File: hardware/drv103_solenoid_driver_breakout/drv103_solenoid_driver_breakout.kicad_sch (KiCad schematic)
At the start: 26 parts, among them J1 DC IN, J2 CONTROL, J3 Solenoid, U1 DRV103U

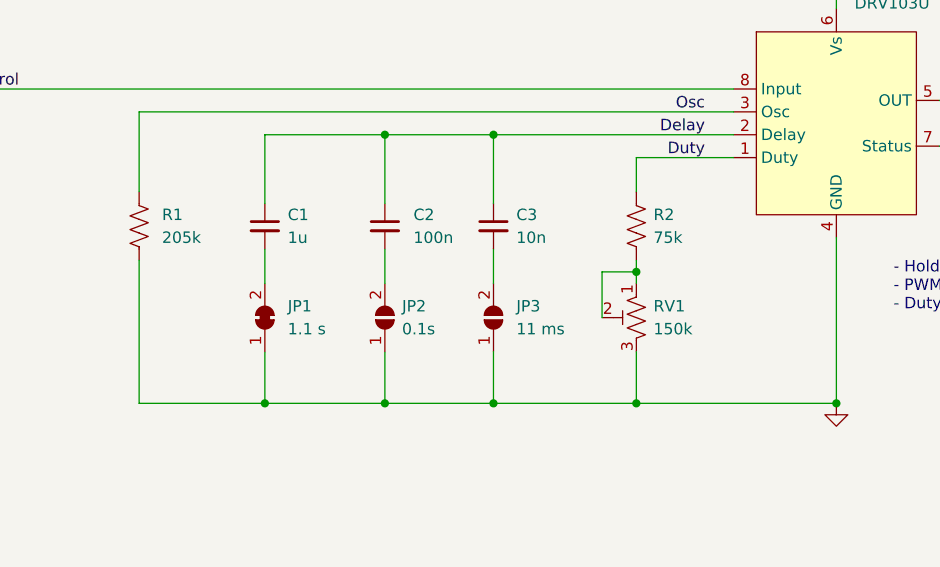
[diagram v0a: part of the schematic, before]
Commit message: Add actual component values
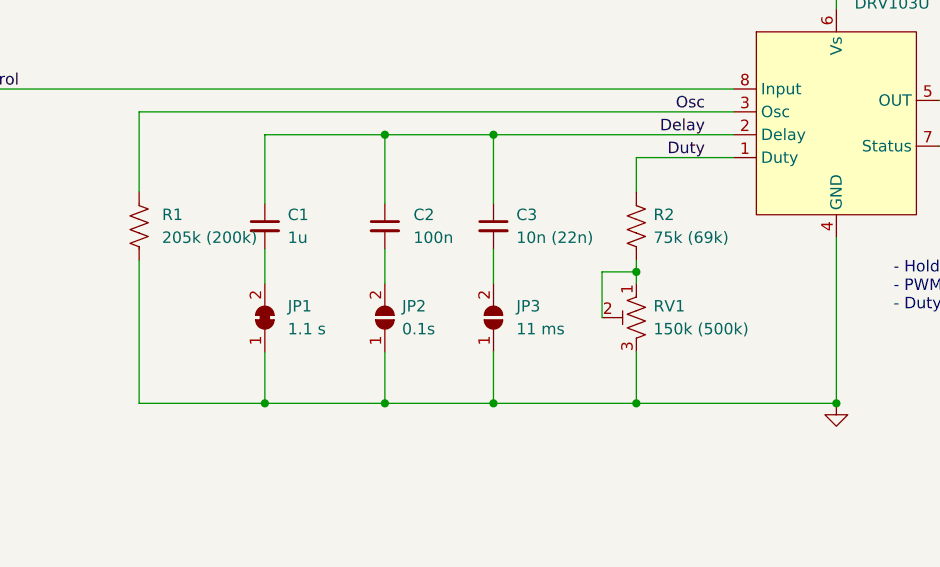
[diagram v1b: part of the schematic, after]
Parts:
- C3: value 10n -> 10n (22n)
- R1: value 205k -> 205k (200k)
- R2: value 75k -> 75k (69k)
- RV1: value 150k -> 150k (500k)
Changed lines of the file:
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@@
       (effects (font (size 1.27 1.27)) (justify right))
     )
-    (property "Value" "75k" (id 1) (at 130.81 106.0449 0)
+    (property "Value" "75k (69k)" (id 1) (at 130.81 106.0449 0)
       (effects (font (size 1.27 1.27)) (justify right))
     )
@@
       (effects (font (size 1.27 1.27)) (justify left))
     )
-    (property "Value" "10n" (id 1) (at 115.57 106.0512 0)
+    (property "Value" "10n (22n)" (id 1) (at 115.57 106.0512 0)
       (effects (font (size 1.27 1.27)) (justify left))
     )
@@
       (effects (font (size 1.27 1.27)) (justify right))
     )
-    (property "Value" "205k" (id 1) (at 76.2 106.0449 0)
+    (property "Value" "205k (200k)" (id 1) (at 76.2 106.0449 0)
       (effects (font (size 1.27 1.27)) (justify right))
     )
@@
       (effects (font (size 1.27 1.27)) (justify right))
     )
-    (property "Value" "150k" (id 1) (at 130.81 116.2049 0)
+    (property "Value" "150k (500k)" (id 1) (at 130.81 116.2049 0)
       (effects (font (size 1.27 1.27)) (justify right))
     )
@@
     )
     (path "/83963a71-109d-4df7-b582-2124aeaa82fb"
-      (reference "C3") (unit 1) (value "10n") (footprint "Capacitor_SMD:C_0603_1608Metric_Pad1.08x0.95mm_HandSolder")
+      (reference "C3") (unit 1) (value "10n (22n)") (footprint "Capacitor_SMD:C_0603_1608Metric_Pad1.08x0.95mm_HandSolder")
     )
     (path "/0f9a5fd2-781b-4164-bc3e-87cb4b11114a"
@@
     )
     (path "/cd5d6ec1-33a5-47ef-8204-cc6fc4d30391"
-      (reference "R1") (unit 1) (value "205k") (footprint "Resistor_SMD:R_0603_1608Metric_Pad0.98x0.95mm_HandSolder")
+      (reference "R1") (unit 1) (value "205k (200k)") (footprint "Resistor_SMD:R_0603_1608Metric_Pad0.98x0.95mm_HandSolder")
     )
     (path "/7beee487-594f-44fd-a6c2-cdf5450be136"
-      (reference "R2") (unit 1) (value "75k") (footprint "Resistor_SMD:R_0603_1608Metric_Pad0.98x0.95mm_HandSolder")
+      (reference "R2") (unit 1) (value "75k (69k)") (footprint "Resistor_SMD:R_0603_1608Metric_Pad0.98x0.95mm_HandSolder")
     )
     (path "/13c5fbb9-842f-451c-8331-bd132b560134"
@@
     )
     (path "/dcabbb36-0452-4b44-a121-6af0d5226253"
-      (reference "RV1") (unit 1) (value "150k") (footprint "Potentiometer_SMD:Potentiometer_Bourns_TC33X_Vertical")
+      (reference "RV1") (unit 1) (value "150k (500k)") (footprint "Potentiometer_SMD:Potentiometer_Bourns_TC33X_Vertical")
     )
     (path "/9a777125-46ce-4c8e-b20c-25eb06956d97"
